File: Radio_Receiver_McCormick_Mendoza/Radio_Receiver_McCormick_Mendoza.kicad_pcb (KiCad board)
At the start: 2 copper layers, 244 parts, among them J1 VBAT, J10 CLK_2, J11 I_LO, J12 Q_LO, J13 I_0, J14 I_180, J15 Q_90, J16 Q_270, J17 I_RAW, J18 Conn_01x02_Female, J19 Conn_01x02_Female, J2 GND, J20 Q_RAW, J21 SDR Out, J23 VDDA, J24 CLK_0, J25 OLED, J26 +5V, J28 Conn_01x01_Pin, J3 VA_3.3, J33 XFIL_IN, J34 XFIL_OUT, J35 3.5mm_Jack, J36 +5V RAW, J37 V_4.5, J38 DAC_FLT, J39 VDD, J4 VA_4.5, J40 DAC_FMT, J41 V_DIV, J42 VDDA/2, J45 CENTER_TAP, J46 3.5mm_Jack, J47 FIL_IN, J5 Conn_Coaxial, J6 Conn_01x02, J7 Micro_SD-TF_PUSH, J8 FIL_OUT, J9 CLK_1, SW1 RotaryEncoder_Switch_MP, SW6 09.03290.01, T1 Transformer_1P_SS, U1 TPS7A2045PDQN, U10 OPA1612AID, U11 INA821ID, U12 PCM1808PWR, U13 SN74CBT3253CDBR, U14 PCM5102A, U2 TPS7A2045PDQN, U3 TPS72733DSER, U4 Pico, U5 Si5351A-B-GT, U6 SN74AC74DR, U8 SN74CBT3253CDBR, U9 INA821ID, Y1 ASTX-H11-24.576MHZ-T

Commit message: Started PCB
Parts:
- moved C35 374.8 mm to (-209.1, 123.7)
- moved C36 374.8 mm to (-209.1, 125.5)
- moved C38 374.8 mm to (-209.1, 127.4)
- moved R7 374.8 mm to (-209.1, 129.2)
- moved R8 374.8 mm to (-209.1, 131.1)
- moved R9 374.8 mm to (-209.1, 132.9)
- moved SW1 374.8 mm to (-227.0, 127.9)
- moved C90 347.2 mm to (-194.1, 141.5)
- moved C91 347.2 mm to (-190.0, 141.1)
- moved J7 347.2 mm to (-187.5, 129.6)
- moved R47 347.2 mm to (-176.8, 124.2)
- moved R49 347.2 mm to (-176.8, 126.4)
- moved R50 347.2 mm to (-176.8, 128.7)
- moved R51 347.2 mm to (-176.8, 130.9)
- moved R54 347.2 mm to (-176.8, 133.2)
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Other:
- board outline added: 100 x 100 mm
- copper layers 2 -> 4
- board text added: "ADC"
- board text added: "Antenna"
- board text added: "Clock Generator"
- board text added: "DAC Audio"
- board text added: "Display/RP2040"
- board text added: "Encoder/SSD"
- board text added: "Mixer"
- board text added: "POWER"

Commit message: Edited PCB Power
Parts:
- moved ON/OFF1 38.0 mm to (-13.5, 29.0)
- moved J4 33.0 mm to (-54.0, 34.0)
- moved J26 26.6 mm to (-33.5, 20.0)
- moved J1 25.7 mm to (-34.5, 35.5), turned to -90 degrees
- moved SW6 15.8 mm to (-38.0, 32.0), turned to -90 degrees
- moved J6 14.4 mm to (-39.0, 36.5)
- moved C12 9.87 mm to (-23.9, 30.5)
- moved C6 9.87 mm to (-23.9, 27.4)
- moved C1 8.32 mm to (-28.9, 47.0), turned to 180 degrees
- moved U2 5.39 mm to (-41.9, 54.8)
- moved U1 2.82 mm to (-28.9, 41.8)
- moved J36 1.00 mm to (-37.5, 20.0)
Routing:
- net (no net): vias 0 -> 4
- added copper zone on In2.Cu, net +3.3VA
- added copper zone on F.Cu, net GND
- added copper zone on In1.Cu, net GND
- added copper zone on F.Cu, net Net-(U1-EN)
- added copper zone on In2.Cu, net VDDA
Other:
- board text added: "Analog"
- board text added: "Digital"

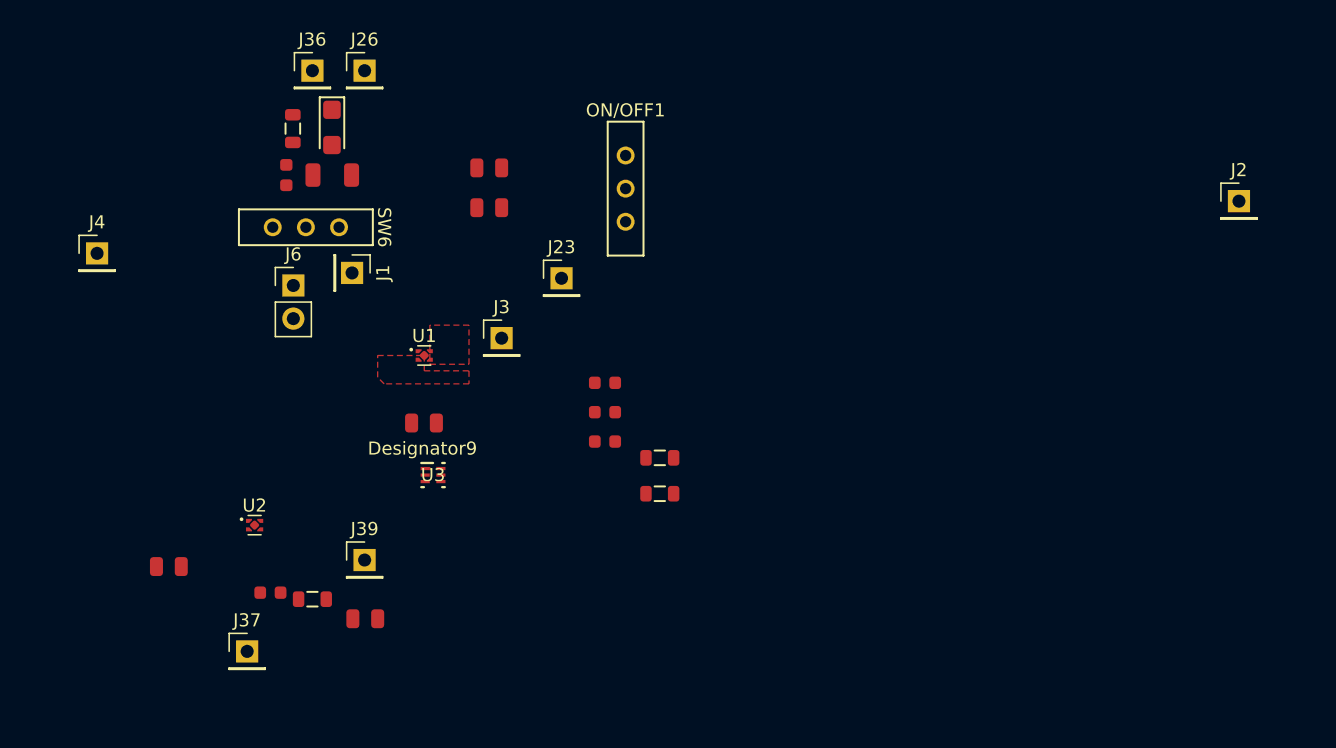
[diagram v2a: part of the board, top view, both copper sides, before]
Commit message: Arranged power components on PCB
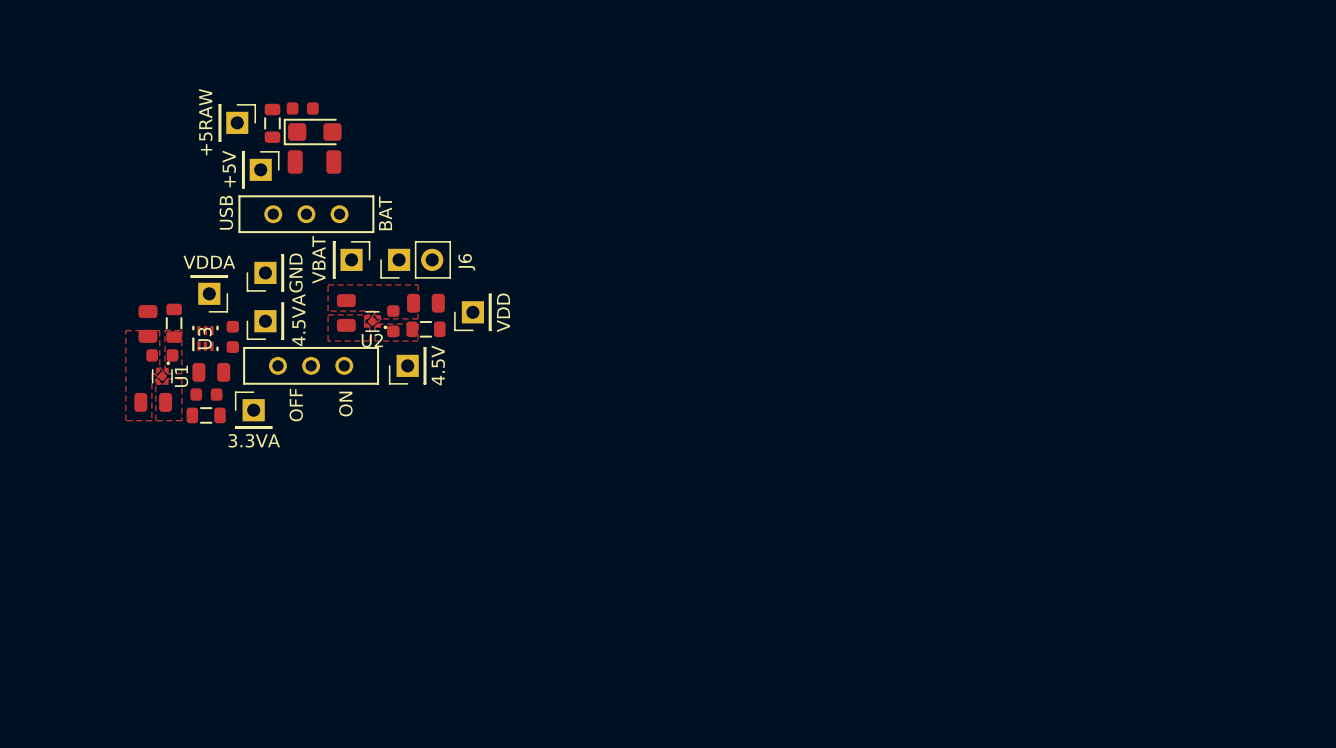
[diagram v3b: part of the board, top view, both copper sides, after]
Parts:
- J3: value VA_3.3 -> 3.3VA
- J36: value +5V RAW -> +5RAW
- J37: value V_4.5 -> 4.5V
- J4: value VA_4.5 -> 4.5VA
- moved J2 74.8 mm to (-41.1, 35.5), turned to 90 degrees
- moved FB18 38.6 mm to (-48.1, 39.4), turned to -90 degrees
- moved FB19 35.3 mm to (-45.6, 46.4), turned to 180 degrees
- moved C32 34.0 mm to (-49.0, 41.8), turned to 180 degrees
- moved C33 30.6 mm to (-45.6, 44.8)
- moved C34 29.6 mm to (-43.6, 40.4), turned to 90 degrees
- moved ON/OFF1 27.7 mm to (-37.6, 42.6), turned to -90 degrees
- moved C12 27.6 mm to (-50.1, 39.4), turned to -90 degrees
- moved J23 27.0 mm to (-45.4, 37.1), turned to 180 degrees
- moved C6 26.4 mm to (-45.2, 43.1)
- moved J37 25.1 mm to (-30.2, 42.6), turned to 90 degrees
- moved C21 24.6 mm to (-28.8, 37.8), turned to 180 degrees
- moved C5 23.7 mm to (-34.9, 38.6), turned to 90 degrees
- moved C40 22.8 mm to (-31.3, 39.2), turned to 90 degrees
- moved FB1 22.4 mm to (-28.8, 39.8)
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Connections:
- C33 pad 1: Net-(J3-Pin_1) -> Net-(U3-OUT)
- C6 pad 1: Net-(J3-Pin_1) -> Net-(U3-OUT)
- C73 pad 1: Net-(C73-Pad1) -> Net-(J26-Pin_1)
- C74 pad 1: Net-(C73-Pad1) -> Net-(J26-Pin_1)
- FB14 pad 2: Net-(C73-Pad1) -> Net-(J26-Pin_1)
- FB19 pad 2: Net-(J3-Pin_1) -> Net-(U3-OUT)
- J26 pad 1: unconnected-(J26-Pin_1-Pad1) -> Net-(J26-Pin_1)
- J3 pad 1: Net-(J3-Pin_1) -> +3.3VA
- SW6 pad 2: Net-(C73-Pad1) -> Net-(J26-Pin_1)
- U3 pad 1: Net-(J3-Pin_1) -> Net-(U3-OUT)
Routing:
- added copper zone on F.Cu, net Net-(J37-Pin_1)
- added copper zone on F.Cu, net Net-(J4-Pin_1)
- removed copper zone on In1.Cu, net GND

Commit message: Arranged antenna and mixer components on PCB
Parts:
- JP1: footprint Connector_PinHeader_2.54mm:PinHeader_1x02_P2.54mm_Vertical -> Jumper:SolderJumper-2_P1.3mm_Bridged2Bar_RoundedPad1.0x1.5mm
- moved J45 363.3 mm to (221.0, 116.4), turned to -90 degrees
- moved C58 356.9 mm to (221.6, 119.3)
- moved T1 349.4 mm to (215.3, 126.6), turned to -90 degrees
- moved J8 348.5 mm to (202.7, 115.6), turned to -90 degrees
- moved J47 336.2 mm to (190.3, 132.6), turned to 90 degrees
- moved JP1 336.1 mm to (190.4, 136.7)
- moved D1 332.8 mm to (190.3, 129.1), turned to 90 degrees
- moved U13 323.6 mm to (208.0, 113.3), turned to -90 degrees
- moved J5 320.4 mm to (182.3, 132.5)
- moved C20 319.2 mm to (211.0, 119.0)
- moved C55 318.5 mm to (198.7, 119.1), turned to -90 degrees
- moved C53 316.3 mm to (194.7, 119.1), turned to 90 degrees
- moved C61 315.7 mm to (203.3, 111.5), turned to -90 degrees
- moved J34 314.2 mm to (213.3, 116.2), turned to 90 degrees
- moved C19 313.6 mm to (196.1, 118.3), turned to -90 degrees
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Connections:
- C19 pad 1: /Antenna/10 -> Net-(U13-2B2)
- C22 pad 1: /Antenna/01 -> Net-(U13-1B3)
- C31 pad 1: /Antenna/10 -> Net-(U13-2B2)
- C55 pad 1: /Antenna/10 -> Net-(U13-2B2)
- C61 pad 1: /Antenna/00 -> Net-(U13-1B1)
- C61 pad 2: /Antenna/00 -> Net-(U13-2B1)
- C67 pad 1: /Antenna/10 -> Net-(U13-1B2)
- J33 pad 1: /Antenna/11 -> Net-(J33-Pin_1)
- J34 pad 1: /Antenna/11 -> Net-(J34-Pin_1)
- L4 pad 2: /Antenna/10 -> Net-(U13-2B2)
- L6 pad 2: /Antenna/01 -> Net-(U13-2B3)
- U13 pad 10: /Antenna/00 -> Net-(U13-2B1)
- U13 pad 11: /Antenna/10 -> Net-(U13-2B2)
- U13 pad 12: /Antenna/01 -> Net-(U13-2B3)
- U13 pad 13: /Antenna/11 -> Net-(J34-Pin_1)
- U13 pad 3: /Antenna/11 -> Net-(J33-Pin_1)
- U13 pad 4: /Antenna/01 -> Net-(U13-1B3)
- U13 pad 5: /Antenna/10 -> Net-(U13-1B2)
- U13 pad 6: /Antenna/00 -> Net-(U13-1B1)

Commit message: Added pico and OLED arrangement to PCB
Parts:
- removed J28: Conn_01x01_Pin, Connector_PinHeader_2.54mm:PinHeader_1x01_P2.54mm_Vertical
- JP14, JP69: moved to B.Cu
- moved R37 404.9 mm to (254.7, 45.0)
- moved C13 403.4 mm to (265.6, 75.5), turned to -90 degrees
- moved D5 402.1 mm to (267.1, 76.2), turned to -90 degrees
- moved D2 399.1 mm to (251.6, 45.3)
- moved C90 398.5 mm to (196.7, 63.7), turned to -90 degrees
- moved C91 396.0 mm to (198.4, 63.7), turned to -90 degrees
- moved R54 385.1 mm to (201.6, 61.9), turned to -90 degrees
- moved R50 383.7 mm to (200.1, 56.9), turned to 90 degrees
- moved J7 381.5 mm to (187.3, 58.5), turned to -90 degrees
- moved R47 380.9 mm to (198.6, 59.7), turned to -90 degrees
- moved JP12 380.6 mm to (257.6, 89.7), turned to -90 degrees
- moved R49 378.9 mm to (196.3, 60.6), turned to -90 degrees
- moved R51 378.3 mm to (194.9, 60.6), turned to 90 degrees
- moved Y1 375.4 mm to (252.6, 93.6), turned to 180 degrees
- moved R36 373.2 mm to (256.0, 86.9)
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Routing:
- net Net-(U6A-~{R}): track 0.00 -> 48.5 mm
- net Net-(J24-Pin_1): track 0.00 -> 23.8 mm
- net Net-(J12-Pin_1): track 0.00 -> 14.9 mm
- net Net-(U6A-Q): track 0.00 -> 5.98 mm
- net +3.3VA: vias 0 -> 2

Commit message: Continue on layout of PCB
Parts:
- moved C59 43.1 mm to (-209.4, 46.6), turned to 90 degrees
- moved J40 42.7 mm to (-213.5, 30.8), turned to 180 degrees
- moved JP10 42.6 mm to (-210.1, 31.4), turned to 0 degrees
- moved C68 38.4 mm to (-205.9, 46.6), turned to 90 degrees
- moved JP6 37.6 mm to (-210.1, 34.0), turned to 180 degrees
- moved J38 35.3 mm to (-213.5, 34.5), turned to -90 degrees
- moved C97 35.2 mm to (-24.5, 185.5), turned to 90 degrees
- moved C85 34.1 mm to (-202.6, 46.5), turned to 90 degrees
- moved e3 33.5 mm to (-216.4, 57.0), turned to -90 degrees
- moved R43 32.7 mm to (-177.8, 28.8), turned to 180 degrees
- moved J42 32.2 mm to (-12.5, 185.9), turned to 180 degrees
- moved R53 31.6 mm to (-4.50, 192.4), turned to 90 degrees
- moved C83 31.0 mm to (-26.5, 185.8), turned to 90 degrees
- moved R52 30.1 mm to (-2.50, 192.5), turned to 90 degrees
- moved C86 30.1 mm to (-199.2, 46.5), turned to 90 degrees
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
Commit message: Placed ADC and DAC onto the PCB layout
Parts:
- JP10, JP6: moved to B.Cu
- moved C42 460.0 mm to (235.5, 87.8)
- moved C43 460.0 mm to (235.5, 85.7)
- moved R10 460.0 mm to (238.2, 85.0)
- moved R29 460.0 mm to (238.2, 88.5)
- moved C59 459.2 mm to (248.6, 80.1)
- moved C68 459.2 mm to (252.1, 80.1)
- moved C86 459.2 mm to (258.8, 80.0)
- moved R45 459.2 mm to (245.4, 82.0)
- moved R48 459.2 mm to (256.2, 76.3)
- moved R6 459.2 mm to (248.2, 84.6)
- moved C49 459.2 mm to (245.7, 83.8)
- moved C85 459.2 mm to (255.3, 80.0)
- moved C89 459.2 mm to (262.2, 80.0)
- moved C96 459.2 mm to (265.2, 80.1)
- moved R33 459.2 mm to (242.2, 81.8)
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
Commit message: Laid out all components to fit on PCB
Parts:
- moved SW1 328.9 mm to (97.4, 74.1), turned to 90 degrees
- moved R7 324.9 mm to (109.4, 65.0), turned to -90 degrees
- moved R8 324.8 mm to (109.4, 67.5), turned to -90 degrees
- moved R9 324.6 mm to (109.4, 70.0), turned to -90 degrees
- moved C35 322.3 mm to (107.9, 65.5), turned to 180 degrees
- moved C36 322.2 mm to (107.9, 68.0), turned to 180 degrees
- moved C38 322.0 mm to (107.9, 70.5), turned to 180 degrees
- moved e5 225.8 mm to (162.0, 84.4), turned to -90 degrees
- moved C52 224.8 mm to (157.9, 84.4), turned to -90 degrees
- moved J21 222.8 mm to (154.3, 91.8), turned to -90 degrees
- moved R31 222.0 mm to (155.9, 84.5), turned to 90 degrees
- moved R48 121.3 mm to (135.1, 83.5), turned to 180 degrees
- moved C61 119.2 mm to (85.8, 131.3)
- moved J34 119.2 mm to (95.8, 136.0)
- moved C20 119.2 mm to (93.5, 138.8)
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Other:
- board text added: "ADC Signal"
- board text removed: "ADC"
